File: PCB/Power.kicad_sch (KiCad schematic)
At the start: 3 parts, among them J1 Power USB C Receptacle

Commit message: IMU done yay
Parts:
- R2, R3: value 5.1k -> 5.1kΩ
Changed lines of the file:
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@@
 			)
 		)
-		(property "Value" "5.1k"
+		(property "Value" "5.1kΩ"
 			(at 48.26 52.07 90)
 			(effects
@@
 			)
 		)
-		(property "Value" "5.1k"
+		(property "Value" "5.1kΩ"
 			(at 48.26 40.64 90)
 			(effects

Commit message: She buck on my converter till I 3.3V DC
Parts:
- added C7: 4.7uF, symbol Device:C
- added C8: 22uF, symbol Device:C
- added L1: 1uH, symbol Device:L
- added R10, R9: 5.1kΩ, symbol Device:R_US
- added U1: TLV62569ADRL, Package_TO_SOT_SMD:SOT-563, symbol Regulator_Switching:TLV62569ADRL
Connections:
- net +5V: now also C7.1, U1.3 (VIN), U1.5 (EN)
- net GND: now also C7.2, C8.2, R10.2, U1.2 (GND)
- new net: L1.1, U1.4 (SW)
- new net: R10.1, R9.2, U1.1 (FB)
- new net Buck_3v3: C8.1, L1.2, R9.1
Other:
- note added: "5V DC to 3.3V DC Buck Converter"

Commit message: add pressure button and R, C, and L footprints
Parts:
- C7, C8: footprint (none) -> Capacitor_SMD:C_1206_3216Metric_Pad1.33x1.80mm_HandSolder
- L1: footprint (none) -> Inductor_SMD:L_1206_3216Metric_Pad1.42x1.75mm_HandSolder
- R10, R2, R3, R9: footprint (none) -> Resistor_SMD:R_1206_3216Metric_Pad1.30x1.75mm_HandSolder
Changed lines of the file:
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@@
 			)
 		)
-		(property "Footprint" ""
+		(property "Footprint" "Inductor_SMD:L_1206_3216Metric_Pad1.42x1.75mm_HandSolder"
 			(at 109.22 34.29 0)
 			(effects
@@
 			)
 		)
-		(property "Footprint" ""
+		(property "Footprint" "Resistor_SMD:R_1206_3216Metric_Pad1.30x1.75mm_HandSolder"
 			(at 48.514 45.974 90)
 			(effects
@@
 			)
 		)
-		(property "Footprint" ""
+		(property "Footprint" "Resistor_SMD:R_1206_3216Metric_Pad1.30x1.75mm_HandSolder"
 			(at 48.514 43.434 90)
 			(effects
@@
 			)
 		)
-		(property "Footprint" ""
+		(property "Footprint" "Capacitor_SMD:C_1206_3216Metric_Pad1.33x1.80mm_HandSolder"
 			(at 125.4252 48.26 0)
 			(effects
@@
 			)
 		)
-		(property "Footprint" ""
+		(property "Footprint" "Resistor_SMD:R_1206_3216Metric_Pad1.30x1.75mm_HandSolder"
 			(at 115.316 38.354 90)
 			(effects
@@
 			)
 		)
-		(property "Footprint" ""
+		(property "Footprint" "Resistor_SMD:R_1206_3216Metric_Pad1.30x1.75mm_HandSolder"
 			(at 115.316 49.784 90)
 			(effects
@@
 			)
 		)
-		(property "Footprint" ""
+		(property "Footprint" "Capacitor_SMD:C_1206_3216Metric_Pad1.33x1.80mm_HandSolder"
 			(at 80.9752 46.99 0)
 			(effects

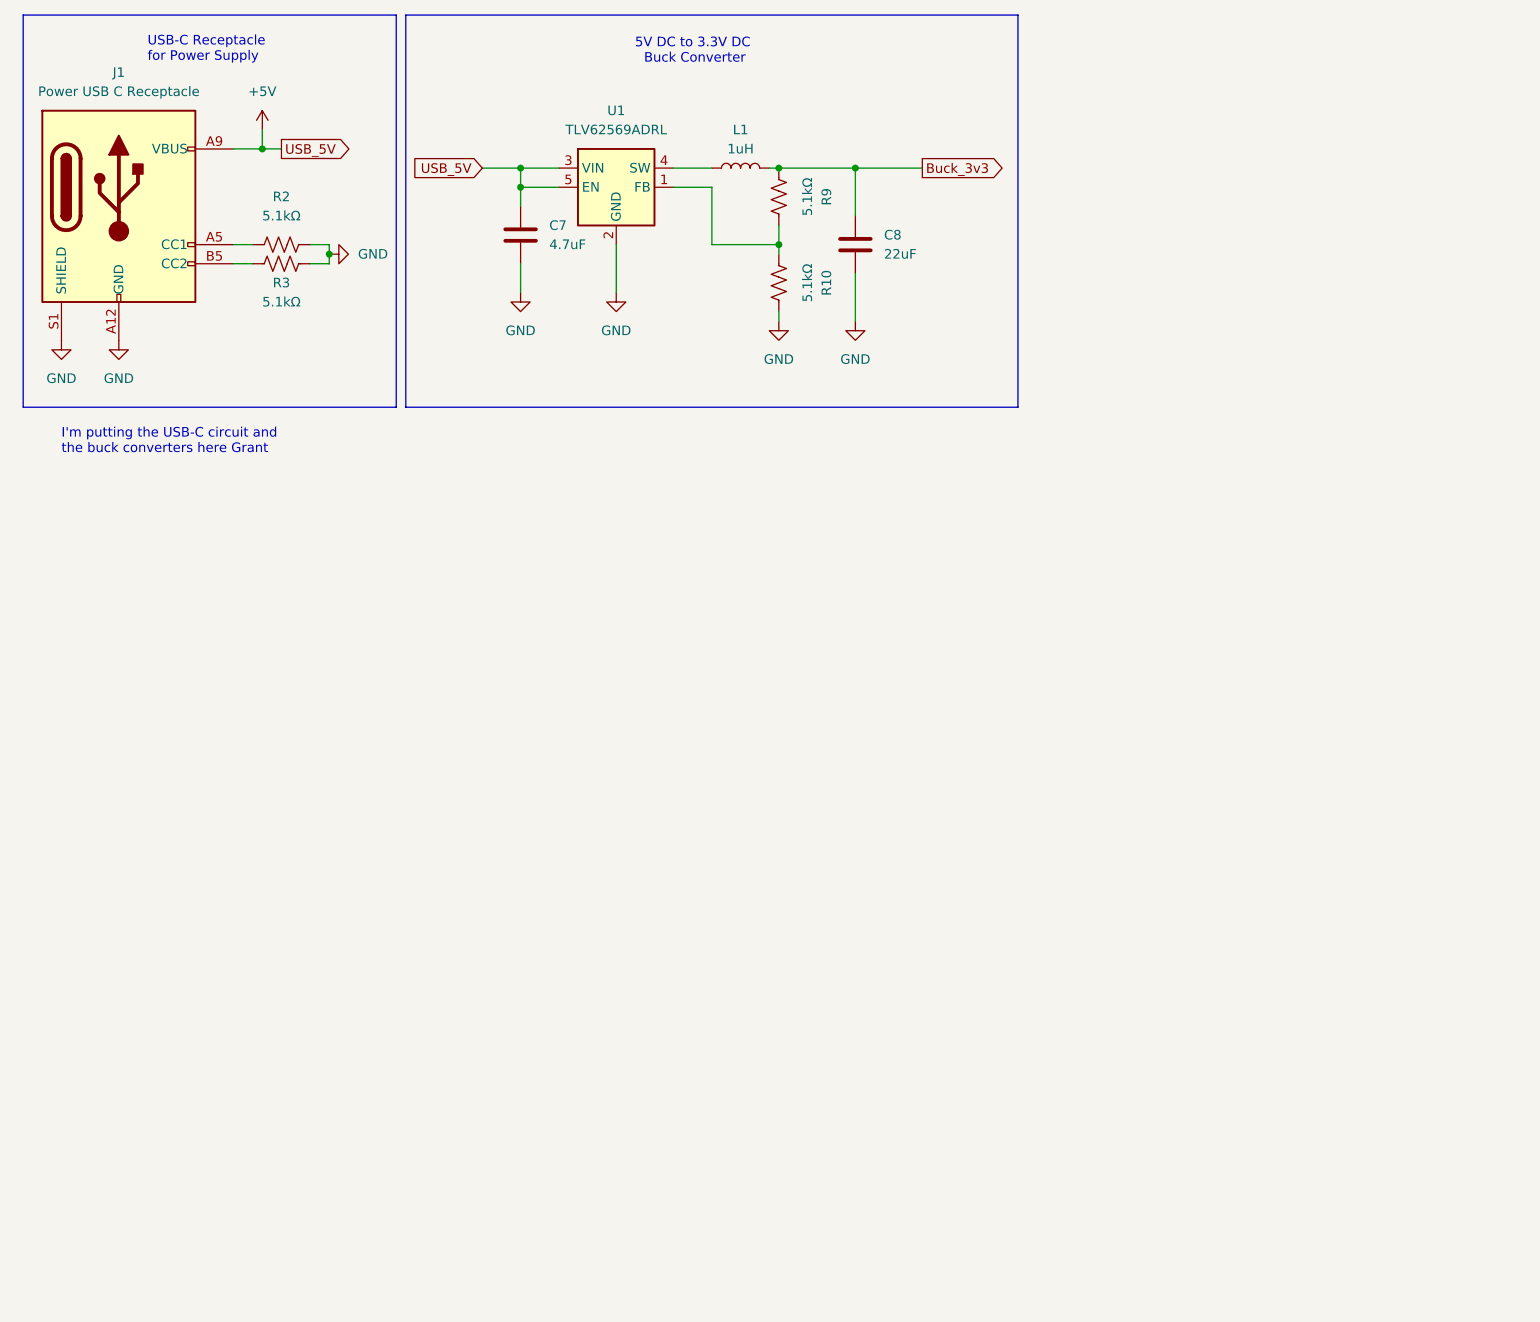
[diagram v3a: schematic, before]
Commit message: Work on adding on board flashing
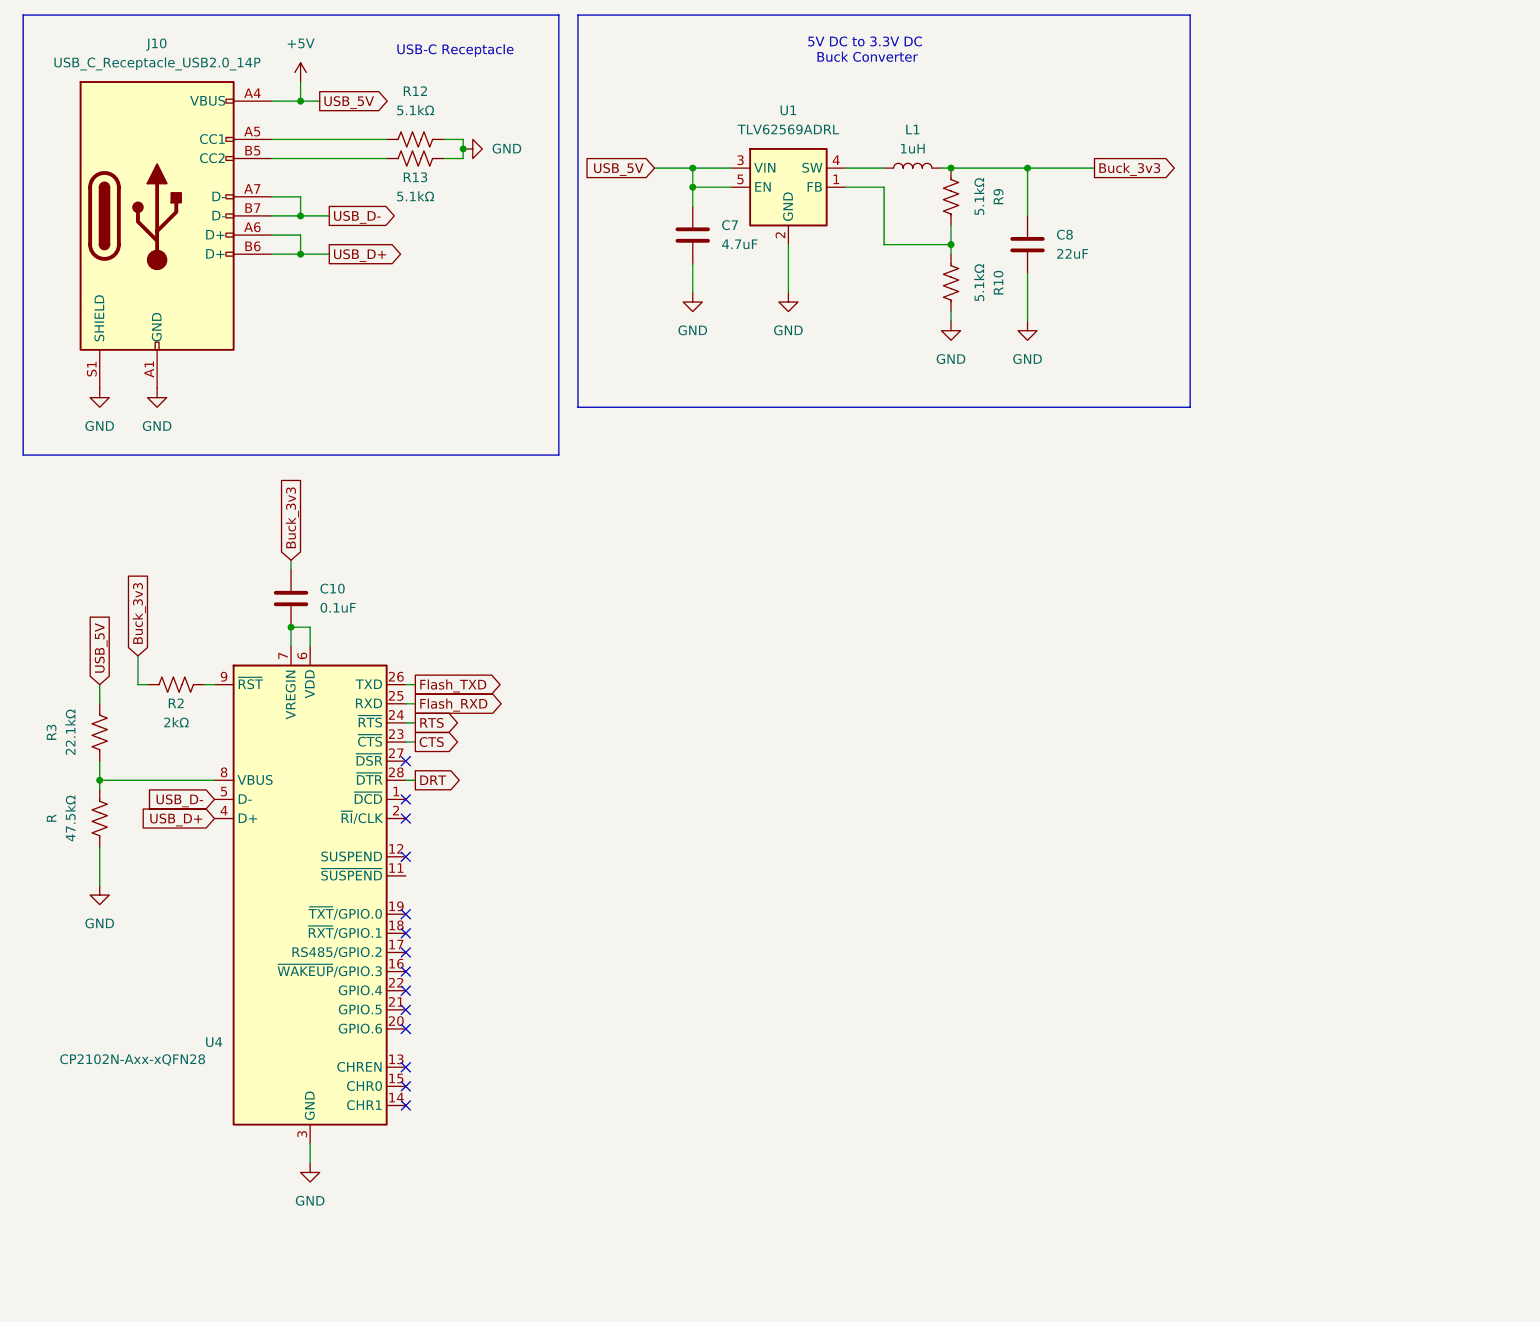
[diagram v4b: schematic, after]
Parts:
- removed J1: Power USB C Receptacle, Connector_USB:USB_C_Receptacle_CNCTech_C-ARA1-AK51X, symbol Connector:USB_C_Receptacle_PowerOnly_6P
- added C10: 0.1uF, Capacitor_SMD:C_1206_3216Metric_Pad1.33x1.80mm_HandSolder, symbol Device:C
- added J10: USB_C_Receptacle_USB2.0_14P, symbol Connector:USB_C_Receptacle_USB2.0_14P
- added R: 47.5kΩ, Resistor_SMD:R_1206_3216Metric_Pad1.30x1.75mm_HandSolder, symbol Device:R_US
- added R12, R13: 5.1kΩ, Resistor_SMD:R_1206_3216Metric_Pad1.30x1.75mm_HandSolder, symbol Device:R_US
- added U4: CP2102N-Axx-xQFN28, Package_DFN_QFN:QFN-28-1EP_5x5mm_P0.5mm_EP3.35x3.35mm, symbol Interface_USB:CP2102N-Axx-xQFN28
- R2: value 5.1kΩ -> 2kΩ
- R3: value 5.1kΩ -> 22.1kΩ
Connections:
- net +5V: now also R3.2, J10.A4 (VBUS), J10.A9 (VBUS), J10.B4 (VBUS), J10.B9 (VBUS)
- net Buck_3v3: now also R2.1, C10.1
- net GND: now also J10.A1 (GND), J10.A12 (GND), J10.B1 (GND), J10.B12 (GND), J10.S1 (SHIELD), R.1, R12.2, R13.2, U4.29 (GND), U4.3 (GND); no longer R2.2, R3.2
- net at R3.1: now also R.2, U4.8 (VBUS)
- new net: J10.B5 (CC2), R13.1
- new net: C10.2, U4.6 (VDD), U4.7 (VREGIN)
- new net: R2.2, U4.9 (~{RST})
- new net: J10.A5 (CC1), R12.1
- new net CTS: U4.23 (~{CTS})
- new net DRT: U4.28 (~{DTR})
- new net Flash_RXD: U4.25 (RXD)
- new net Flash_TXD: U4.26 (TXD)
- new net RTS: U4.24 (~{RTS})
- new net USB_D+: J10.A6 (D+), J10.B6 (D+), U4.4 (D+)
- new net USB_D-: J10.A7 (D-), J10.B7 (D-), U4.5 (D-)
- no-connect marks 0 -> 14
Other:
- note added: "USB-C Receptacle"
- note removed: "I'm putting the USB-C circuit and the buck converters here Grant"
- note removed: "USB-C Receptacle for Power Supply"
- moved on the sheet: C7, C8, L1, R10, R9, U1

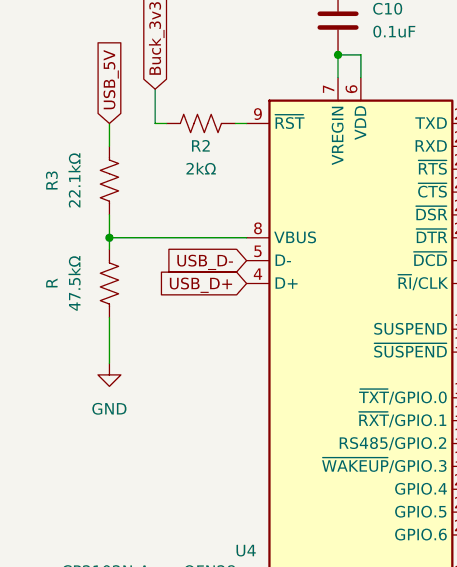
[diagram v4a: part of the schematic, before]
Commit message: Created push button footprint
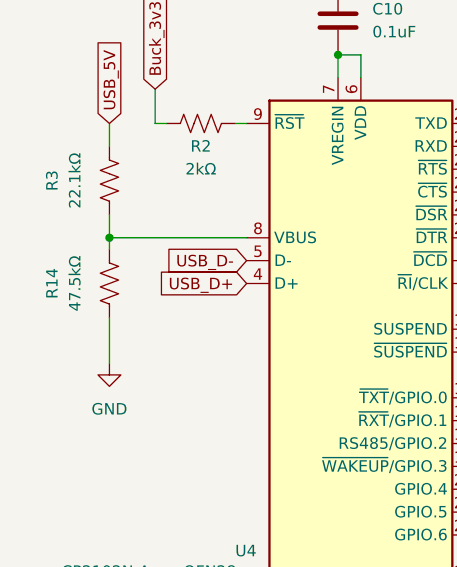
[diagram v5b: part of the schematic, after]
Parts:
- renumbered R to R14
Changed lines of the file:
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@@
 		(on_board yes)
 		(dnp no)
-		(property "Reference" "R"
+		(property "Reference" "R14"
 			(at 17.78 120.65 90)
 			(effects
@@
 			(project "Smart_Backpack"
 				(path "/38abc652-c887-4ef7-a45f-d93ca7f4b2d6/2d9f036a-c70f-4011-9e39-88b7ded8327f"
-					(reference "R")
+					(reference "R14")
 					(unit 1)
 				)
